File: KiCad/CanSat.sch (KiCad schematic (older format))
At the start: 0 parts

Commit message: Update schematic
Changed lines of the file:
@@
 $EndDescr
 $Sheet
-S 3500 2100 1500 1000
+S 3500 2100 1000 1000
 U 5FCA6470
 F0 "RPi CM4" 50
@@
 F3 "SCL" O L 3500 3550 50
 F4 "DS_EXTERNAL" B L 3500 4200 50
-F5 "LED_DATA" O L 3500 3950 50
-F6 "DEPLOY" I L 3500 4050 50
+F5 "LED_DATA" I L 3500 3950 50
+F6 "DEPLOY" O L 3500 4050 50
 F7 "DS_ONBOARD" B L 3500 4300 50
 F8 "RADIO_INT" O L 3500 4600 50
@@
 F12 "RADIO_RST" O R 3050 4700 50
 F13 "RADIO_INT" I R 3050 4600 50
+F14 "LED_DATA" O R 3050 3950 50
+F15 "DEPLOY" I R 3050 4050 50
+F16 "DS_TEMP" B R 3050 4200 50
+F17 "RUN_PG" B R 3050 2750 50
+F18 "GLOBAL_EN" O R 3050 2650 50
 $EndSheet
+Wire Wire Line
+	3500 4200 3400 4200
+Wire Wire Line
+	3500 4300 3400 4300
+Wire Wire Line
+	3400 4300 3400 4200
+Connection ~ 3400 4200
+Wire Wire Line
+	3400 4200 3050 4200
+Wire Wire Line
+	3500 4050 3050 4050
+Wire Wire Line
+	3500 3950 3050 3950
+Wire Wire Line
+	3050 2650 3500 2650
+Wire Wire Line
+	3050 2750 3500 2750
 $EndSCHEMATC

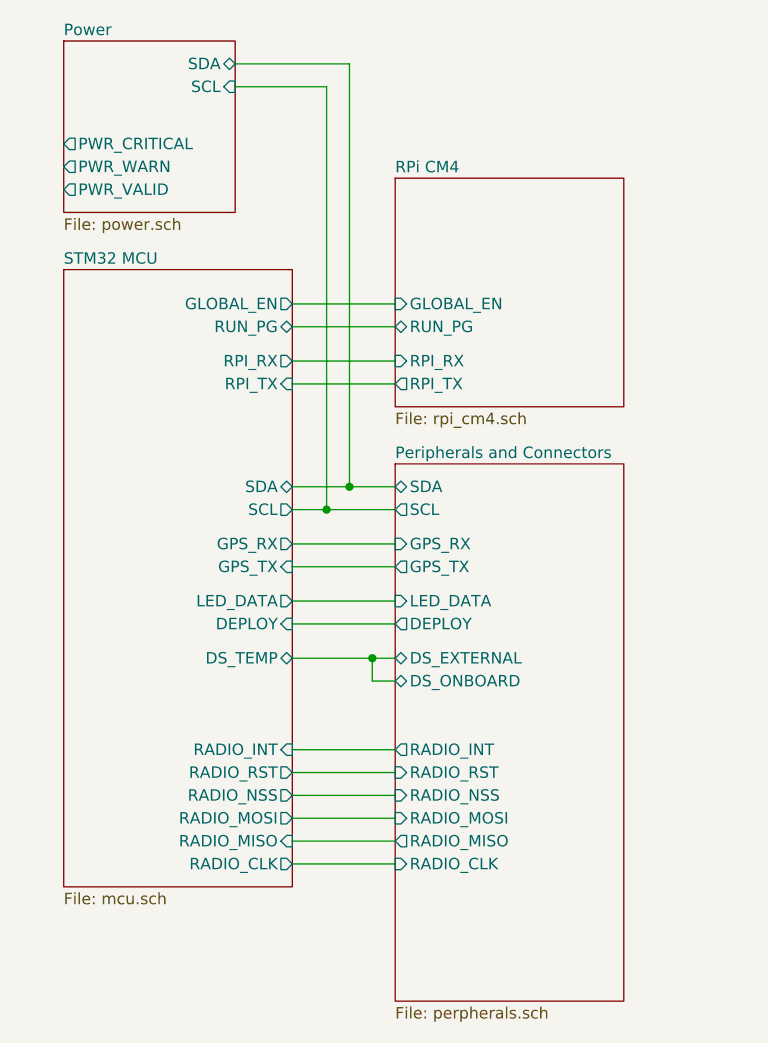
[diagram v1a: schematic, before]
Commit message: Finalized schematic and created S/F associations
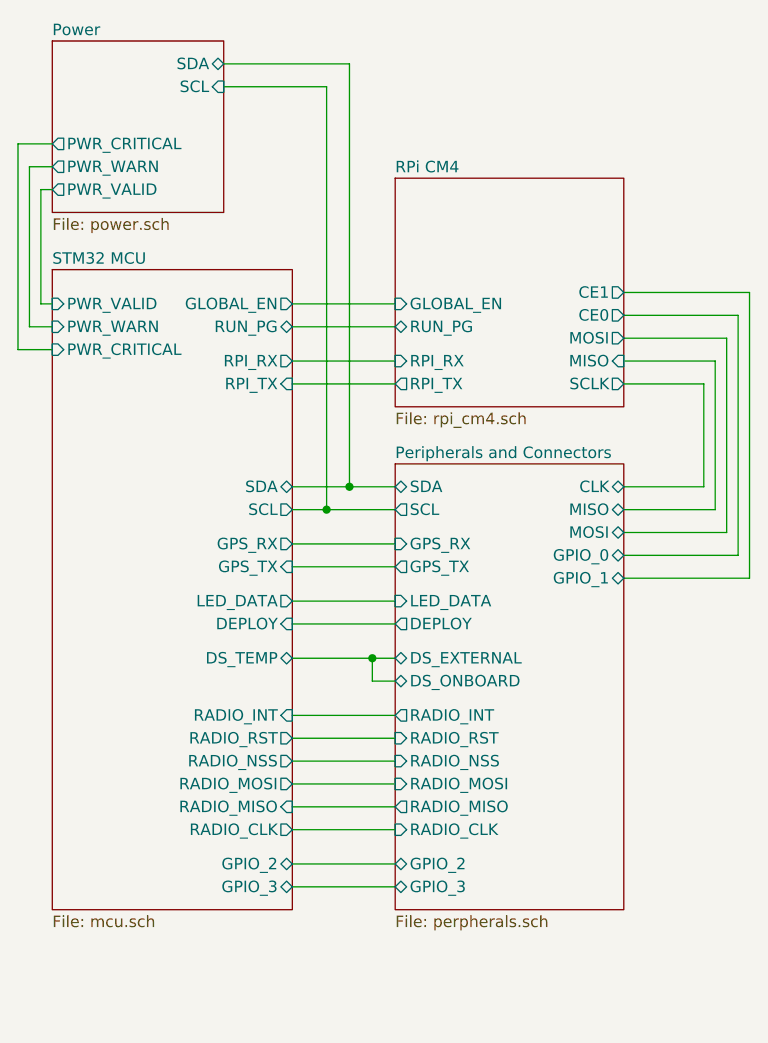
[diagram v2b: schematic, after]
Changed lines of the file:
@@
 $EndDescr
+$Sheet
+S 3500 3350 1000 1950
+U 5FCA658C
+F0 "Peripherals and Connectors" 50
+F1 "perpherals.sch" 50
+F2 "SDA" B L 3500 3450 50
+F3 "SCL" O L 3500 3550 50
+F4 "DS_EXTERNAL" B L 3500 4200 50
+F5 "LED_DATA" I L 3500 3950 50
+F6 "DEPLOY" O L 3500 4050 50
+F7 "DS_ONBOARD" B L 3500 4300 50
+F8 "RADIO_INT" O L 3500 4450 50
+F9 "RADIO_RST" I L 3500 4550 50
+F10 "RADIO_NSS" I L 3500 4650 50
+F11 "RADIO_CLK" I L 3500 4950 50
+F12 "RADIO_MOSI" I L 3500 4750 50
+F13 "RADIO_MISO" O L 3500 4850 50
+F14 "GPS_RX" I L 3500 3700 50
+F15 "GPS_TX" O L 3500 3800 50
+F16 "MISO" B R 4500 3550 50
+F17 "MOSI" B R 4500 3650 50
+F18 "CLK" B R 4500 3450 50
+F19 "GPIO_0" B R 4500 3750 50
+F20 "GPIO_1" B R 4500 3850 50
+F21 "GPIO_2" B L 3500 5100 50
+F22 "GPIO_3" B L 3500 5200 50
+$EndSheet
+Wire Wire Line
+	3500 4200 3400 4200
+Wire Wire Line
+	3500 4300 3400 4300
+Wire Wire Line
+	3400 4300 3400 4200
+Connection ~ 3400 4200
+$Sheet
+S 2000 1500 750  750
+U 5FCA604B
+F0 "Power" 50
+F1 "power.sch" 50
+F2 "PWR_VALID" O L 2000 2150 50
+F3 "PWR_WARN" O L 2000 2050 50
+F4 "PWR_CRITICAL" O L 2000 1950 50
+F5 "SCL" I R 2750 1700 50
+F6 "SDA" B R 2750 1600 50
+$EndSheet
+Wire Wire Line
+	1950 2150 2000 2150
+Wire Wire Line
+	1950 2150 1950 2650
+Wire Wire Line
+	1950 2650 2000 2650
+Wire Wire Line
+	1900 2050 1900 2750
+Wire Wire Line
+	1900 2750 2000 2750
+Wire Wire Line
+	1900 2050 2000 2050
+Wire Wire Line
+	1850 1950 1850 2850
+Wire Wire Line
+	1850 2850 2000 2850
+Wire Wire Line
+	1850 1950 2000 1950
+Wire Wire Line
+	2750 1700 3200 1700
+Wire Wire Line
+	3300 3450 3500 3450
+Connection ~ 3300 3450
+Wire Wire Line
+	3300 1600 3300 3450
+Wire Wire Line
+	3200 3550 3500 3550
+Connection ~ 3200 3550
+Wire Wire Line
+	3200 1700 3200 3550
+Wire Wire Line
+	4500 3000 4850 3000
+Wire Wire Line
+	4850 3000 4850 3450
+Wire Wire Line
+	4850 3450 4500 3450
+Wire Wire Line
+	4500 2900 4900 2900
+Wire Wire Line
+	4900 2900 4900 3550
+Wire Wire Line
+	4900 3550 4500 3550
+Wire Wire Line
+	4500 2800 4950 2800
+Wire Wire Line
+	4950 2800 4950 3650
+Wire Wire Line
+	4950 3650 4500 3650
+Wire Wire Line
+	4500 2700 5000 2700
+Wire Wire Line
+	5000 2700 5000 3750
+Wire Wire Line
+	5000 3750 4500 3750
+Wire Wire Line
+	4500 2600 5050 2600
+Wire Wire Line
+	5050 2600 5050 3850
+Wire Wire Line
+	5050 3850 4500 3850
+Wire Wire Line
+	3050 2650 3500 2650
+Wire Wire Line
+	3050 2750 3500 2750
+Wire Wire Line
+	3400 4200 3050 4200
+Wire Wire Line
+	3500 4050 3050 4050
+Wire Wire Line
+	3500 3950 3050 3950
+Wire Wire Line
+	3500 4450 3050 4450
+Wire Wire Line
+	3050 4550 3500 4550
+Wire Wire Line
+	3500 4650 3050 4650
+Wire Wire Line
+	3050 3550 3200 3550
+Wire Wire Line
+	3050 3450 3300 3450
+Wire Wire Line
+	3500 4750 3050 4750
+Wire Wire Line
+	3500 4850 3050 4850
+Wire Wire Line
+	3500 4950 3050 4950
+Wire Wire Line
+	3050 3800 3500 3800
+Wire Wire Line
+	3050 3700 3500 3700
+Wire Wire Line
+	3500 2900 3050 2900
+Wire Wire Line
+	3500 3000 3050 3000
+$Sheet
+S 2000 2500 1050 2800
+U 5FCA62D1
+F0 "STM32 MCU" 50
+F1 "mcu.sch" 50
+F2 "RPI_TX" I R 3050 3000 50
+F3 "RPI_RX" O R 3050 2900 50
+F4 "GPS_RX" O R 3050 3700 50
+F5 "GPS_TX" I R 3050 3800 50
+F6 "RADIO_CLK" O R 3050 4950 50
+F7 "RADIO_MISO" I R 3050 4850 50
+F8 "RADIO_MOSI" O R 3050 4750 50
+F9 "SDA" B R 3050 3450 50
+F10 "SCL" O R 3050 3550 50
+F11 "RADIO_NSS" O R 3050 4650 50
+F12 "RADIO_RST" O R 3050 4550 50
+F13 "RADIO_INT" I R 3050 4450 50
+F14 "LED_DATA" O R 3050 3950 50
+F15 "DEPLOY" I R 3050 4050 50
+F16 "DS_TEMP" B R 3050 4200 50
+F17 "RUN_PG" B R 3050 2750 50
+F18 "GLOBAL_EN" O R 3050 2650 50
+F19 "PWR_CRITICAL" I L 2000 2850 50
+F20 "PWR_WARN" I L 2000 2750 50
+F21 "PWR_VALID" I L 2000 2650 50
+F22 "GPIO_2" B R 3050 5100 50
+F23 "GPIO_3" B R 3050 5200 50
+$EndSheet
+Wire Wire Line
+	2750 1600 3300 1600
+Wire Wire Line
+	3050 5100 3500 5100
+Wire Wire Line
+	3050 5200 3500 5200
 $Sheet
 S 3500 2100 1000 1000
@@
 F4 "RUN_PG" B L 3500 2750 50
 F5 "GLOBAL_EN" I L 3500 2650 50
+F6 "MOSI" O R 4500 2800 50
+F7 "MISO" I R 4500 2900 50
+F8 "SCLK" O R 4500 3000 50
+F9 "CE0" O R 4500 2700 50
+F10 "CE1" O R 4500 2600 50
 $EndSheet
-$Sheet
-S 2050 1500 750  750
-U 5FCA604B
-F0 "Power" 50
-F1 "power.sch" 50
-F2 "PWR_VALID" O L 2050 2150 50
-F3 "PWR_WARN" O L 2050 2050 50
-F4 "PWR_CRITICAL" O L 2050 1950 50
-F5 "SCL" I R 2800 1700 50
-F6 "SDA" B R 2800 1600 50
-$EndSheet
-Wire Wire Line
-	3500 2900 3050 2900
-Wire Wire Line
-	3500 3000 3050 3000
-Wire Wire Line
-	3050 3450 3300 3450
-$Sheet
-S 3500 3350 1000 2350
-U 5FCA658C
-F0 "Peripherals and Connectors" 50
-F1 "perpherals.sch" 50
-F2 "SDA" B L 3500 3450 50
-F3 "SCL" O L 3500 3550 50
-F4 "DS_EXTERNAL" B L 3500 4200 50
-F5 "LED_DATA" I L 3500 3950 50
-F6 "DEPLOY" O L 3500 4050 50
-F7 "DS_ONBOARD" B L 3500 4300 50
-F8 "RADIO_INT" O L 3500 4600 50
-F9 "RADIO_RST" I L 3500 4700 50
-F10 "RADIO_NSS" I L 3500 4800 50
-F11 "RADIO_CLK" I L 3500 5100 50
-F12 "RADIO_MOSI" I L 3500 4900 50
-F13 "RADIO_MISO" O L 3500 5000 50
-F14 "GPS_RX" I L 3500 3700 50
-F15 "GPS_TX" O L 3500 3800 50
-$EndSheet
-Wire Wire Line
-	3500 4600 3050 4600
-Wire Wire Line
-	3050 4700 3500 4700
-Wire Wire Line
-	3500 4800 3050 4800
-Wire Wire Line
-	3500 4900 3050 4900
-Wire Wire Line
-	3500 5000 3050 5000
-Wire Wire Line
-	3500 5100 3050 5100
-Wire Wire Line
-	3050 3700 3500 3700
-Wire Wire Line
-	3050 3800 3500 3800
-Wire Wire Line
-	2800 1600 3300 1600
-Wire Wire Line
-	3300 1600 3300 3450
-Connection ~ 3300 3450
-Wire Wire Line
-	3300 3450 3500 3450
-Wire Wire Line
-	2800 1700 3200 1700
-Wire Wire Line
-	3200 3550 3500 3550
-Connection ~ 3200 3550
-Wire Wire Line
-	3200 1700 3200 3550
-Wire Wire Line
-	3050 3550 3200 3550
-$Sheet
-S 2050 2500 1000 2700
-U 5FCA62D1
-F0 "STM32 MCU" 50
-F1 "mcu.sch" 50
-F2 "RPI_TX" I R 3050 3000 50
-F3 "RPI_RX" O R 3050 2900 50
-F4 "GPS_RX" O R 3050 3700 50
-F5 "GPS_TX" I R 3050 3800 50
-F6 "RADIO_CLK" O R 3050 5100 50
-F7 "RADIO_MISO" I R 3050 5000 50
-F8 "RADIO_MOSI" O R 3050 4900 50
-F9 "SDA" B R 3050 3450 50
-F10 "SCL" O R 3050 3550 50
-F11 "RADIO_NSS" O R 3050 4800 50
-F12 "RADIO_RST" O R 3050 4700 50
-F13 "RADIO_INT" I R 3050 4600 50
-F14 "LED_DATA" O R 3050 3950 50
-F15 "DEPLOY" I R 3050 4050 50
-F16 "DS_TEMP" B R 3050 4200 50
-F17 "RUN_PG" B R 3050 2750 50
-F18 "GLOBAL_EN" O R 3050 2650 50
-$EndSheet
-Wire Wire Line
-	3500 4200 3400 4200
-Wire Wire Line
-	3500 4300 3400 4300
-Wire Wire Line
-	3400 4300 3400 4200
-Connection ~ 3400 4200
-Wire Wire Line
-	3400 4200 3050 4200
-Wire Wire Line
-	3500 4050 3050 4050
-Wire Wire Line
-	3500 3950 3050 3950
-Wire Wire Line
-	3050 2650 3500 2650
-Wire Wire Line
-	3050 2750 3500 2750
 $EndSCHEMATC
